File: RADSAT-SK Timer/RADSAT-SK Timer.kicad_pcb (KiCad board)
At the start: 2 copper layers, 95.9 x 90 mm, 108 parts, among them J101 Conn_02x26_Odd_Even, J103 Conn_02x26_Odd_Even, J201 Conn_01x04, J203 Conn_01x02, Q101 IRLML2060, Q102 IRLML2060, Q103 IRLML2060, Q104 IRLML2060, Q105 IRLML2060, Q106 IRLML2060, Q107 IRLML2060, Q108 IRLML2060, Q109 IRLML2060, Q201 IRLML2060, SW205 SW_Push, SW206 SW_Push, U101 LM397MF, U102 LM397MF, U103 LM397MF, U104 CD4052B, U201 LP2980IM5-5.0, U202 LTC3440EMSPBF, U203 TPS3700DDCR

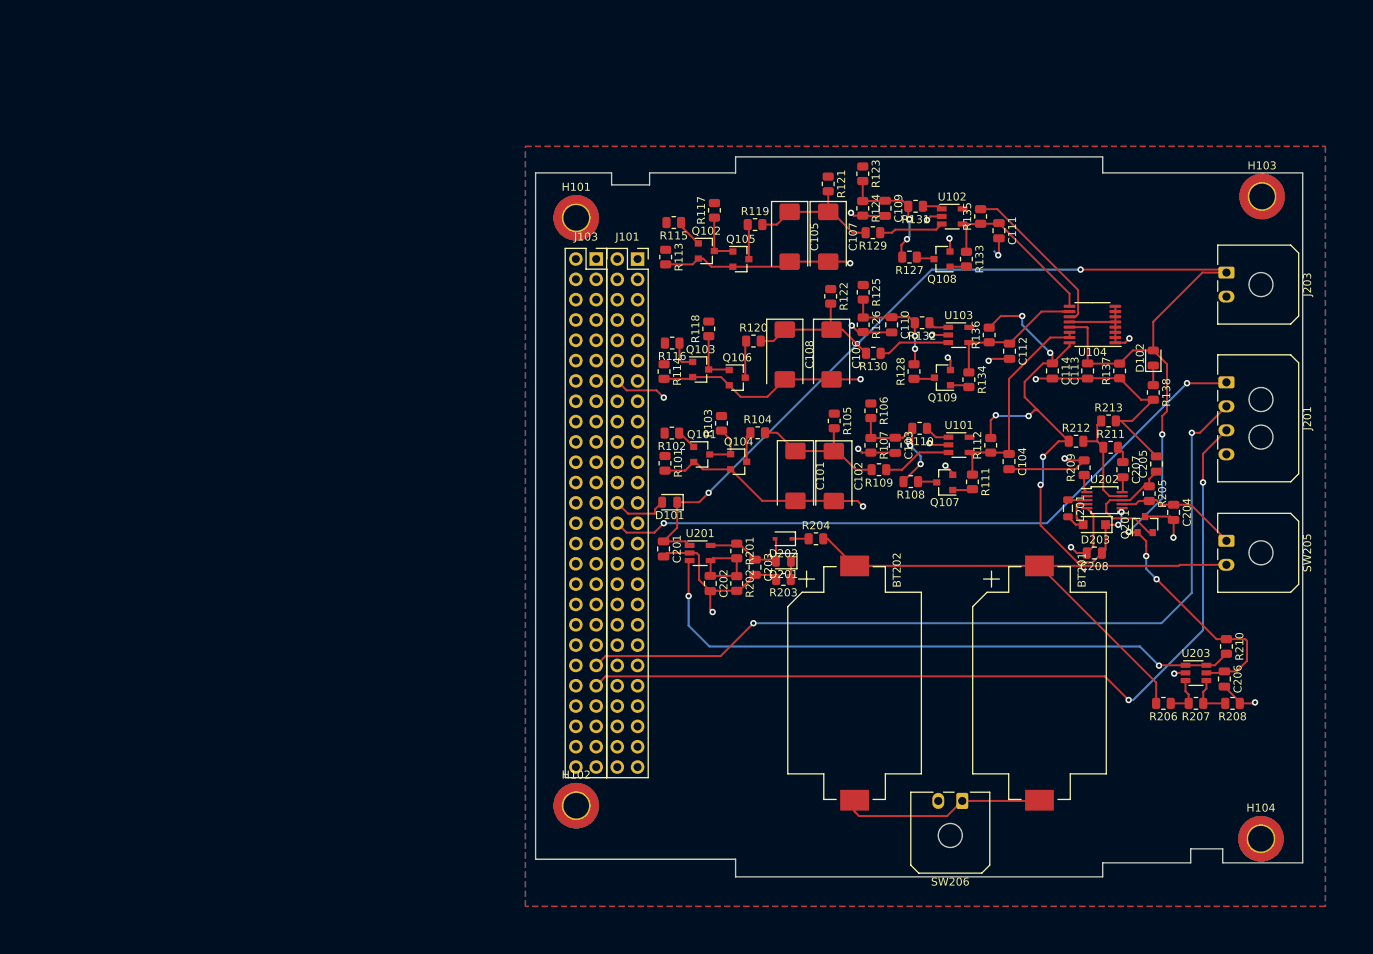
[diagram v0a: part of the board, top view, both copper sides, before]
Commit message: Pc bresize (#7)
* PCB has been resized and the layer redone to fit the new shape, assumed a cent                                                                                                                                                                                  red stack for the main connector. No rounded edges.

* figured out how to do rounded corners also pull request test

* Rounded corners X24
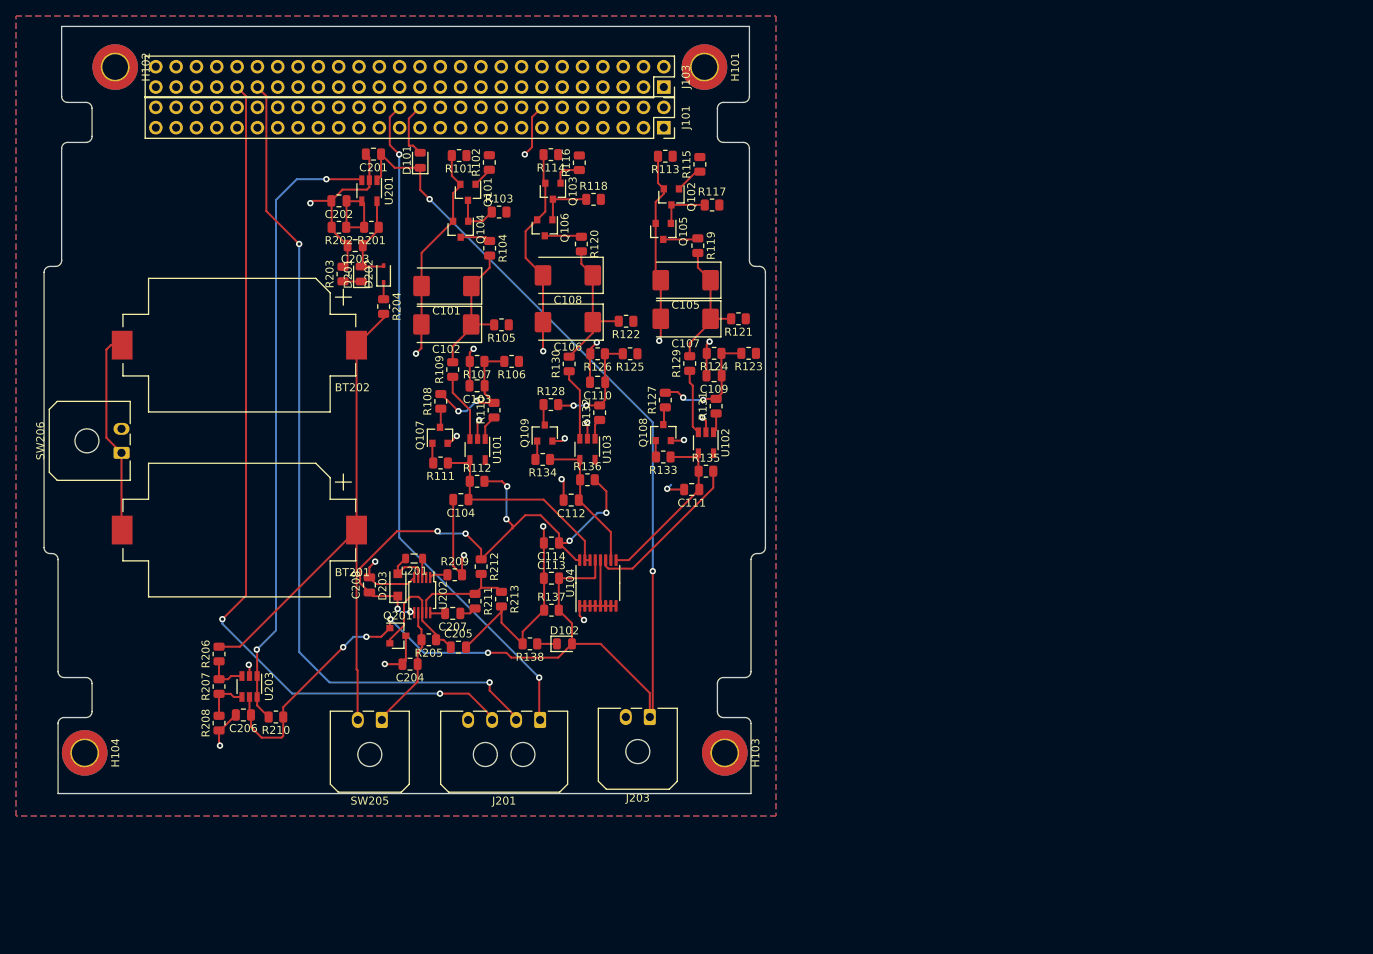
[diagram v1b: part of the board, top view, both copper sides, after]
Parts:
- moved H104 147.4 mm to (39.9, 140.8), turned to 270 degrees
- moved R208 126.7 mm to (56.7, 137.1), turned to 90 degrees
- moved C206 122.7 mm to (59.7, 136.1), turned to 180 degrees
- moved R207 122.1 mm to (56.7, 132.5), turned to 90 degrees
- moved R210 119.1 mm to (63.8, 136.3), turned to 180 degrees
- moved U203 118.3 mm to (60.5, 132.5), turned to 270 degrees
- moved R206 118.2 mm to (56.7, 128.5), turned to 90 degrees
- moved SW206 113.7 mm to (44.5, 103.3), turned to 90 degrees
- moved H102 108.8 mm to (43.7, 55.1), turned to 270 degrees
- moved SW205 107.9 mm to (77.0, 136.7), turned to 180 degrees
- moved BT201 101.8 mm to (59.2, 113.0), turned to 180 degrees
- moved C204 97.3 mm to (80.6, 129.7), turned to 180 degrees
- moved H103 96.7 mm to (119.9, 140.8), turned to 270 degrees
- moved J201 95.6 mm to (96.8, 136.7), turned to 180 degrees
- moved Q201 94.4 mm to (79.1, 126.2), turned to 0 degrees
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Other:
- board size 95.9 x 90 mm -> 90.2 x 95.9 mm

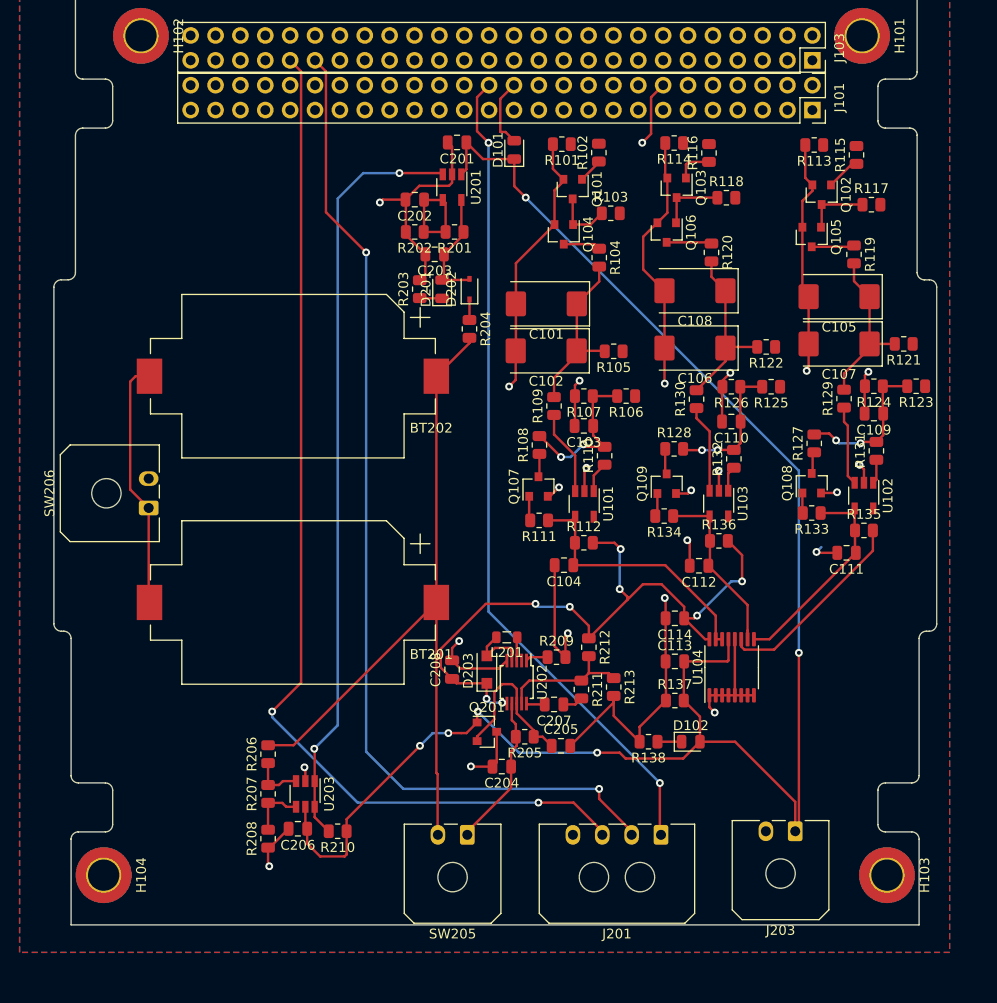
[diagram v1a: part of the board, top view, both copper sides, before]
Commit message: deleted files for a battery holder that we are not using, -had added it myself-  rearanged some of the layout to get outer edge for ports, changed to df13 hirose ports, added dummy usb connector.
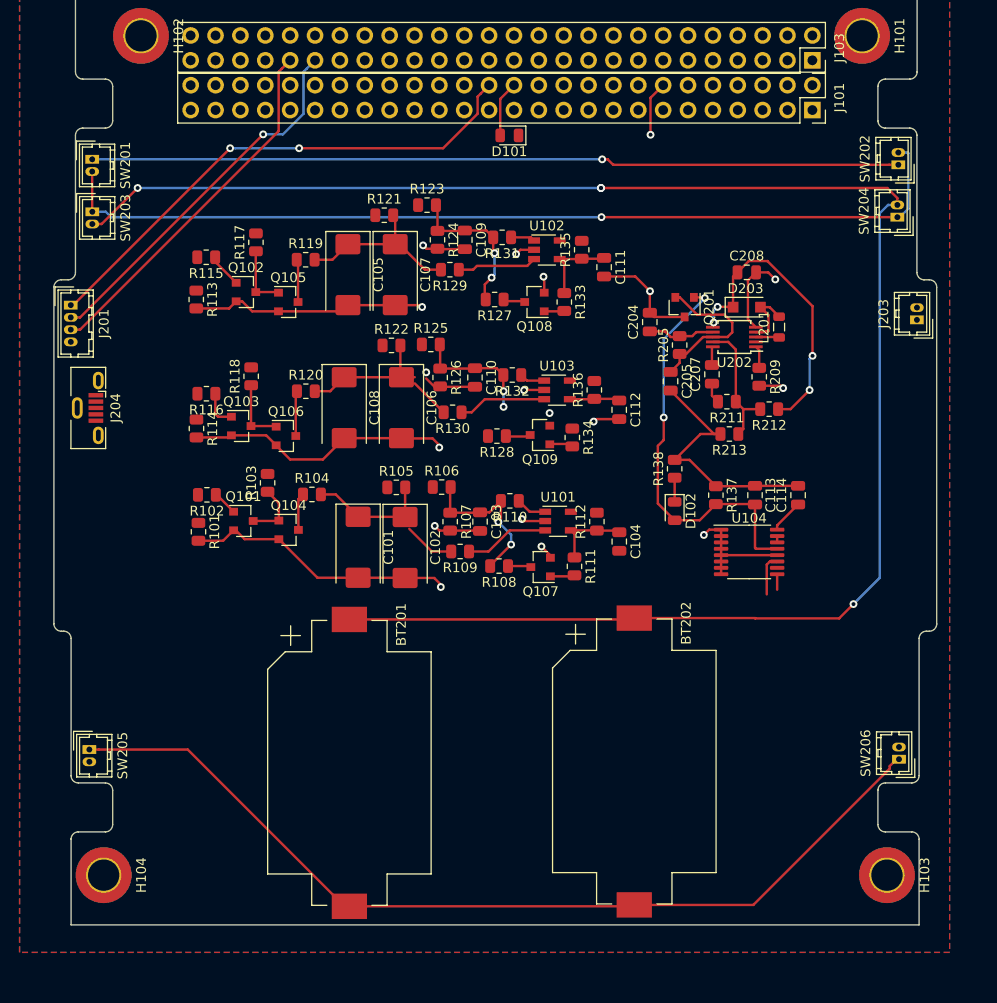
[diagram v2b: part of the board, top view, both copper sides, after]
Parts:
- removed C201: 1uF, Capacitor_SMD:C_0805_2012Metric
- removed C202: 7pF, Capacitor_SMD:C_0805_2012Metric
- removed C203: 2.2uF, Capacitor_SMD:C_0805_2012Metric
- removed C206: 0.1uF, Capacitor_SMD:C_0805_2012Metric
- removed D201: LED, LED_SMD:LED_0805_2012Metric
- removed D202: RB751V40T1G, Diode_SMD:D_SOD-323
- removed R201: 76.8k, Resistor_SMD:R_0805_2012Metric
- removed R202: 51.1k, Resistor_SMD:R_0805_2012Metric
- removed R203: 1k, Resistor_SMD:R_0805_2012Metric
- removed R204: 560, Resistor_SMD:R_0805_2012Metric
- removed R206: 604K, Resistor_SMD:R_0805_2012Metric
- removed R207: 49.9k, Resistor_SMD:R_0805_2012Metric
- removed R208: 100k, Resistor_SMD:R_0805_2012Metric
- removed R210: 10k, Resistor_SMD:R_0805_2012Metric
- removed U201: LP2980IM5-5.0, Package_TO_SOT_SMD:TSOT-23-5
- removed U203: TPS3700DDCR, Package_TO_SOT_SMD:TSOT-23-6
- added J204: USB_B_Micro, Connector_USB:USB_Micro-B_Molex-105133-0001, F.Cu at (38.3, 93.1)
- added SW201: SW_Push, Connector_Hirose:Hirose_DF13-02P-1.25DSA_1x02_P1.25mm_Vertical, F.Cu at (38.7, 67.7)
- added SW202: SW_Push, Connector_Hirose:Hirose_DF13-02P-1.25DSA_1x02_P1.25mm_Vertical, F.Cu at (121.1, 68.2)
- added SW203: SW_Push, Connector_Hirose:Hirose_DF13-02P-1.25DSA_1x02_P1.25mm_Vertical, F.Cu at (38.8, 73.0)
- added SW204: SW_Push, Connector_Hirose:Hirose_DF13-02P-1.25DSA_1x02_P1.25mm_Vertical, F.Cu at (121.0, 73.6)
- J201: footprint Connector_Molex:Molex_Micro-Fit_3.0_43650-0400_1x04_P3.00mm_Horizontal -> Connector_Hirose:Hirose_DF13-04P-1.25DSA_1x04_P1.25mm_Vertical
- J203, SW205, SW206: footprint Connector_Molex:Molex_Micro-Fit_3.0_43650-0200_1x02_P3.00mm_Horizontal -> Connector_Hirose:Hirose_DF13-02P-1.25DSA_1x02_P1.25mm_Vertical
- moved J201 81.0 mm to (36.5, 82.6), turned to 270 degrees
- moved SW206 80.8 mm to (121.2, 129.0)
- moved R115 67.2 mm to (50.4, 77.7), turned to 180 degrees
- moved R113 65.1 mm to (49.4, 82.0), turned to 270 degrees
- moved R117 63.0 mm to (55.5, 76.2), turned to 90 degrees
- moved Q102 59.6 mm to (54.4, 81.3), turned to 0 degrees
- moved R116 56.9 mm to (50.4, 91.6), turned to 180 degrees
- moved R114 56.8 mm to (49.4, 95.2), turned to 270 degrees
- moved R119 56.0 mm to (60.5, 77.9), turned to 0 degrees
- moved R121 54.7 mm to (68.6, 73.4), turned to 0 degrees
- moved R101 54.3 mm to (49.6, 105.7), turned to 270 degrees
- moved Q105 53.9 mm to (58.8, 82.3), turned to 0 degrees
- moved J203 53.7 mm to (123.0, 84.1), turned to 90 degrees
- moved R123 53.3 mm to (72.9, 72.4), turned to 0 degrees
- moved R102 53.1 mm to (50.5, 102.0), turned to 180 degrees
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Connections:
- J101 pad 1: Net-(J101-Pad1) -> (no net)
- J101 pad 10: Net-(J101-Pad10) -> (no net)
- J101 pad 11: Net-(J101-Pad11) -> (no net)
- J101 pad 12: Net-(J101-Pad12) -> (no net)
- J101 pad 13: Net-(J101-Pad13) -> (no net)
- J101 pad 15: Net-(J101-Pad15) -> (no net)
- J101 pad 16: Net-(J101-Pad16) -> (no net)
- J101 pad 17: Net-(J101-Pad17) -> (no net)
- J101 pad 18: Net-(J101-Pad18) -> (no net)
- J101 pad 19: Net-(J101-Pad19) -> (no net)
- J101 pad 2: Net-(J101-Pad2) -> (no net)
- J101 pad 20: Net-(J101-Pad20) -> (no net)
- J101 pad 21: Net-(J101-Pad21) -> (no net)
- J101 pad 22: Net-(J101-Pad22) -> (no net)
- J101 pad 23: Net-(J101-Pad23) -> (no net)
- J101 pad 24: Net-(J101-Pad24) -> (no net)
- J101 pad 25: Net-(J101-Pad25) -> (no net)
- J101 pad 27: Net-(J101-Pad27) -> (no net)
- J101 pad 29: Net-(J101-Pad29) -> (no net)
- J101 pad 3: Net-(J101-Pad3) -> (no net)
- J101 pad 30: Net-(J101-Pad30) -> (no net)
- J101 pad 31: Net-(J101-Pad31) -> (no net)
- J101 pad 32: Net-(J101-Pad32) -> (no net)
- J101 pad 33: Net-(J101-Pad33) -> (no net)
- J101 pad 34: Net-(J101-Pad34) -> (no net)
- J101 pad 35: Net-(J101-Pad35) -> (no net)
- J101 pad 36: Net-(J101-Pad36) -> (no net)
- J101 pad 37: Net-(J101-Pad37) -> (no net)
- J101 pad 38: Net-(J101-Pad38) -> (no net)
- J101 pad 39: Net-(J101-Pad39) -> (no net)
- J101 pad 4: Net-(J101-Pad4) -> (no net)
- J101 pad 40: Net-(J101-Pad40) -> (no net)
- J101 pad 41: Net-(J101-Pad41) -> (no net)
- J101 pad 42: Net-(J101-Pad42) -> (no net)
- J101 pad 43: Net-(J101-Pad43) -> (no net)
- J101 pad 44: Net-(J101-Pad44) -> (no net)
- J101 pad 45: Net-(J101-Pad45) -> (no net)
- J101 pad 46: Net-(J101-Pad46) -> (no net)
- J101 pad 47: Net-(J101-Pad47) -> (no net)
- J101 pad 48: Net-(J101-Pad48) -> (no net)
- J101 pad 49: Net-(J101-Pad49) -> (no net)
- J101 pad 5: Net-(J101-Pad5) -> (no net)
- J101 pad 50: Net-(J101-Pad50) -> (no net)
- J101 pad 51: Net-(J101-Pad51) -> (no net)
- J101 pad 52: Net-(J101-Pad52) -> (no net)
- J101 pad 6: Net-(J101-Pad6) -> (no net)
- J101 pad 7: Net-(J101-Pad7) -> (no net)
- J101 pad 8: Net-(J101-Pad8) -> (no net)
- J101 pad 9: Net-(J101-Pad9) -> (no net)
- J103 pad 1: Net-(J103-Pad1) -> (no net)
- J103 pad 10: Net-(J103-Pad10) -> (no net)
- J103 pad 11: Net-(J103-Pad11) -> (no net)
- J103 pad 12: Net-(J103-Pad12) -> (no net)
- J103 pad 13: Net-(J103-Pad13) -> (no net)
- J103 pad 14: Net-(J103-Pad14) -> (no net)
- J103 pad 15: Net-(J103-Pad15) -> (no net)
- J103 pad 16: Net-(J103-Pad16) -> (no net)
- J103 pad 17: Net-(J103-Pad17) -> (no net)
- J103 pad 18: Net-(J103-Pad18) -> (no net)
- J103 pad 19: Net-(J103-Pad19) -> (no net)
- J103 pad 2: Net-(J103-Pad2) -> (no net)
- J103 pad 20: Net-(J103-Pad20) -> (no net)
- J103 pad 21: Net-(J103-Pad21) -> (no net)
- J103 pad 22: Net-(J103-Pad22) -> (no net)
- J103 pad 23: Net-(J103-Pad23) -> (no net)
- J103 pad 24: Net-(J103-Pad24) -> (no net)
- J103 pad 25: Net-(J103-Pad25) -> (no net)
- J103 pad 26: Net-(J103-Pad26) -> (no net)
- J103 pad 27: Net-(J103-Pad27) -> (no net)
- J103 pad 28: Net-(J103-Pad28) -> (no net)
- J103 pad 29: Net-(J103-Pad29) -> (no net)
- J103 pad 3: Net-(J103-Pad3) -> (no net)
- J103 pad 30: Net-(J103-Pad30) -> (no net)
- J103 pad 31: Net-(J103-Pad31) -> (no net)
- J103 pad 32: Net-(J103-Pad32) -> (no net)
- J103 pad 33: Net-(J103-Pad33) -> (no net)
- J103 pad 34: Net-(J103-Pad34) -> (no net)
- J103 pad 35: Net-(J103-Pad35) -> (no net)
- J103 pad 36: Net-(J103-Pad36) -> (no net)
- J103 pad 37: Net-(J103-Pad37) -> (no net)
- J103 pad 38: Net-(J103-Pad38) -> (no net)
- J103 pad 39: Net-(J103-Pad39) -> (no net)
- J103 pad 4: Net-(J103-Pad4) -> (no net)
- J103 pad 40: Net-(J103-Pad40) -> (no net)
- J103 pad 42: Net-(J103-Pad42) -> (no net)
- J103 pad 44: Net-(J103-Pad44) -> (no net)
- J103 pad 45: Net-(J103-Pad45) -> (no net)
- J103 pad 46: Net-(J103-Pad46) -> (no net)
- J103 pad 47: Net-(J103-Pad47) -> (no net)
- J103 pad 48: Net-(J103-Pad48) -> (no net)
- J103 pad 49: Net-(J103-Pad49) -> (no net)
- J103 pad 5: Net-(J103-Pad5) -> (no net)
- J103 pad 50: Net-(J103-Pad50) -> (no net)
- J103 pad 51: Net-(J103-Pad51) -> (no net)
- J103 pad 52: Net-(J103-Pad52) -> (no net)
- J103 pad 6: Net-(J103-Pad6) -> (no net)
- J103 pad 7: Net-(J103-Pad7) -> (no net)
- J103 pad 8: Net-(J103-Pad8) -> (no net)
- J103 pad 9: Net-(J103-Pad9) -> (no net)
- SW205 pad 1: Net-(C204-Pad1) -> Net-(BT201-Pad2)
- SW205 pad 2: Net-(BT201-Pad1) -> GND
- U202 pad 2: Net-(U202-Pad2) -> (no net)
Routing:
- net BUS_EN: track 176.9 -> 42.2 mm, vias 6 -> 2
- net Net-(BT201-Pad1): track 75.1 -> 180.3 mm, vias 0 -> 4
- net Net-(SW201-Pad2): track 0.00 -> 94.8 mm, vias 0 -> 1
- net CHRG_ON-OFF: track 78.1 -> 0.00 mm, vias 2 -> 0
- net Net-(C204-Pad1): track 15.4 -> 89.5 mm, vias 0 -> 1
- net Net-(BT201-Pad2): track 25.6 -> 95.7 mm
- net I2C_CLK: track 107.4 -> 37.3 mm, vias 2 -> 0
- net I2C_DATA: track 103.9 -> 38.3 mm, vias 2 -> 1
- net +BATT: track 89.5 -> 38.2 mm, vias 8 -> 4
- net GND: track 212.3 -> 172.2 mm, vias 23 -> 18
- net +3V3: track 84.4 -> 53.1 mm
- net Timer_A_out: track 27.7 -> 8.59 mm
- net Timer_C_out: track 18.0 -> 5.18 mm
- net Timer_B_out: track 22.3 -> 9.83 mm
- net Net-(C203-Pad1): track 12.0 -> 0.00 mm
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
